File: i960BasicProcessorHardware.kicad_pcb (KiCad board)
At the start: 4 copper layers, 169.9 x 169.8 mm, 72 parts, among them J1 Conn_01x08, J10 Conn_01x03, J11 Conn_01x03, J12 Conn_01x06, J13 Conn_01x11, J14 Conn_02x39_Odd_Even, J4 Conn_02x05_Odd_Even, J5 Conn_02x05_Odd_Even, J6 Conn_02x05_Odd_Even, J9 Conn_02x16_Odd_Even, U1 74HC245, U10 Adafruit_FeatherWing (PSRAM F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, U11 Adafruit_FeatherWing (PSRAM F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, U12 74LS125, U13 74LS04, U14 74LS08, U15 74LS174, U16 SN74LVC245AN, U17 74LS174, U18 ATtiny861-20PU, U19 ATtiny861-20PU, U2 80960Sx, U3 MCP23S17_SP, U4 MCP23S17_SP, U5 74HC245, U6 74HC573, U7 74HC573, U8 MCP23S17_SP, U9 MCP23S17_SP

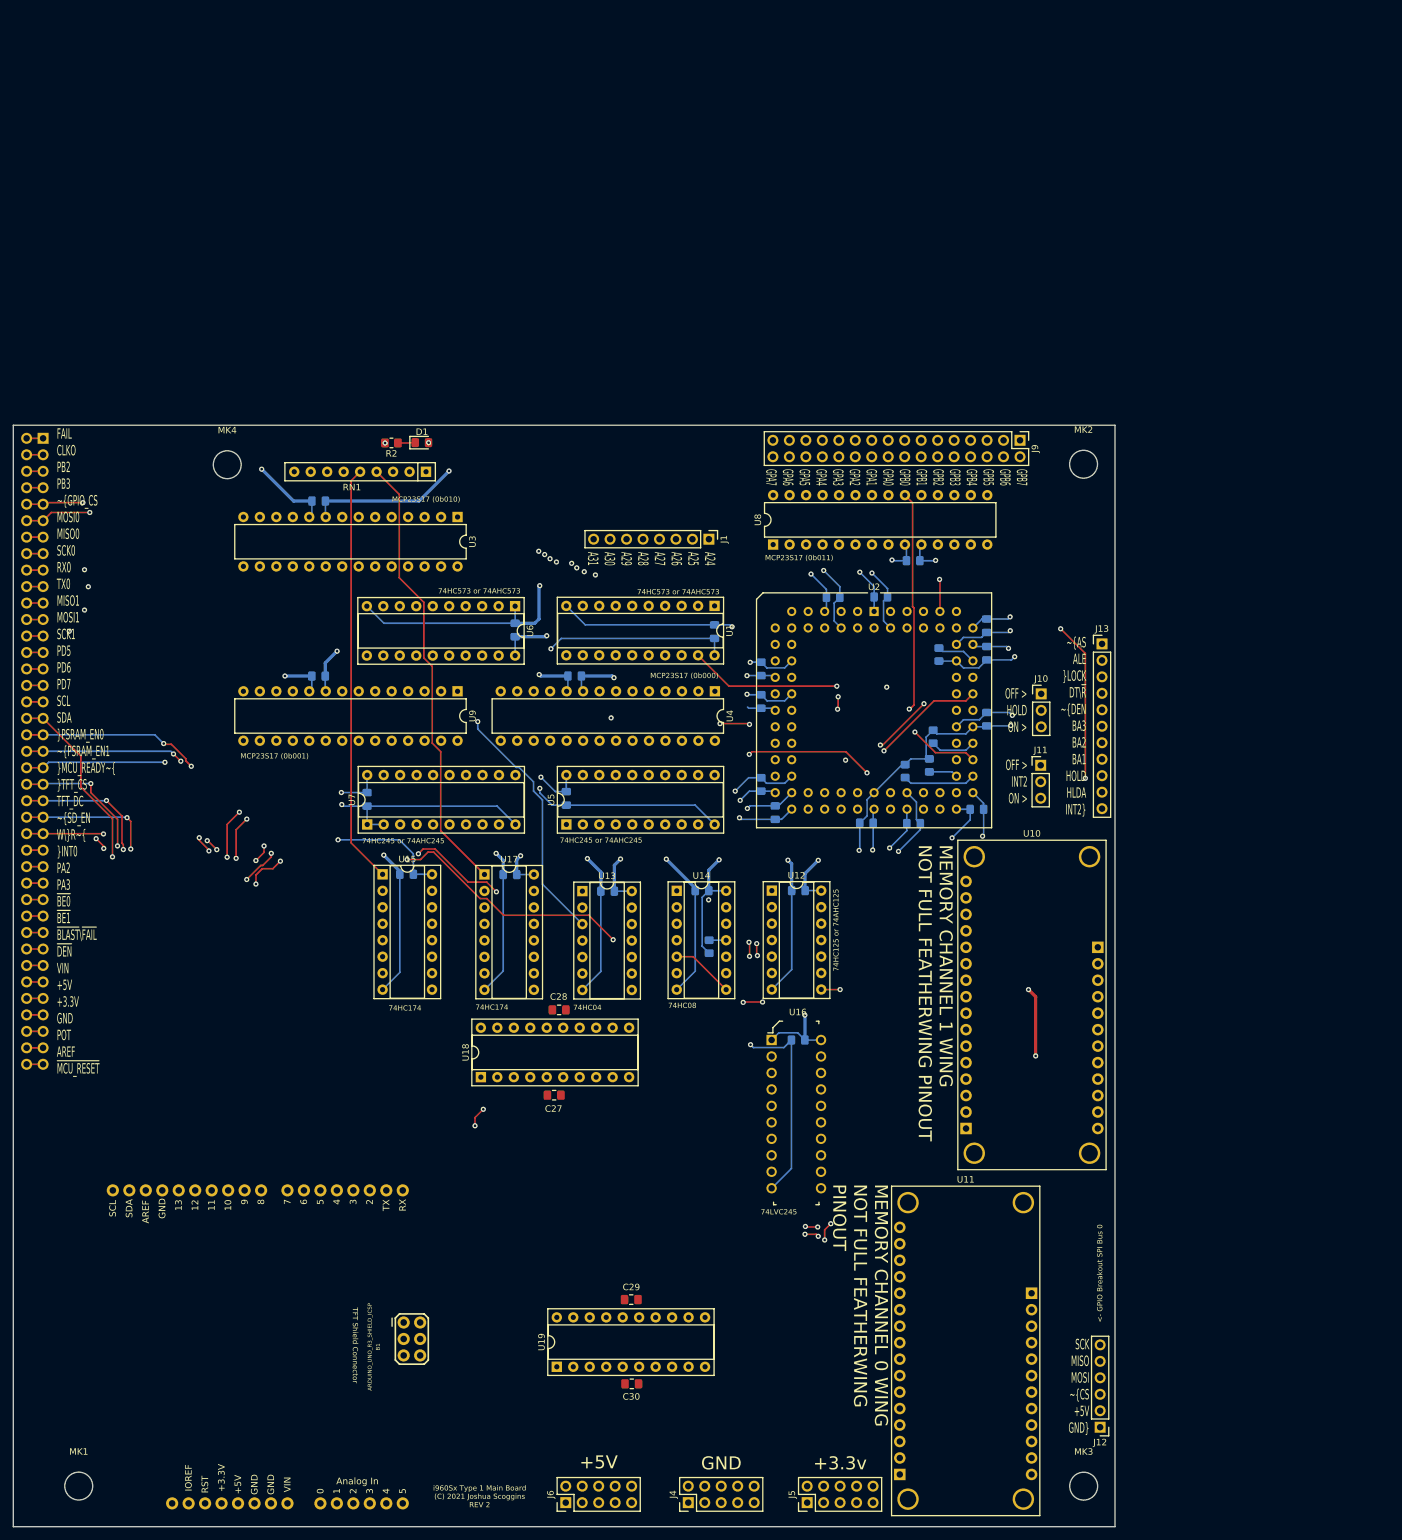
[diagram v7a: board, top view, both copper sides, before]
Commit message: start moving the 74lvc245 to free up some space
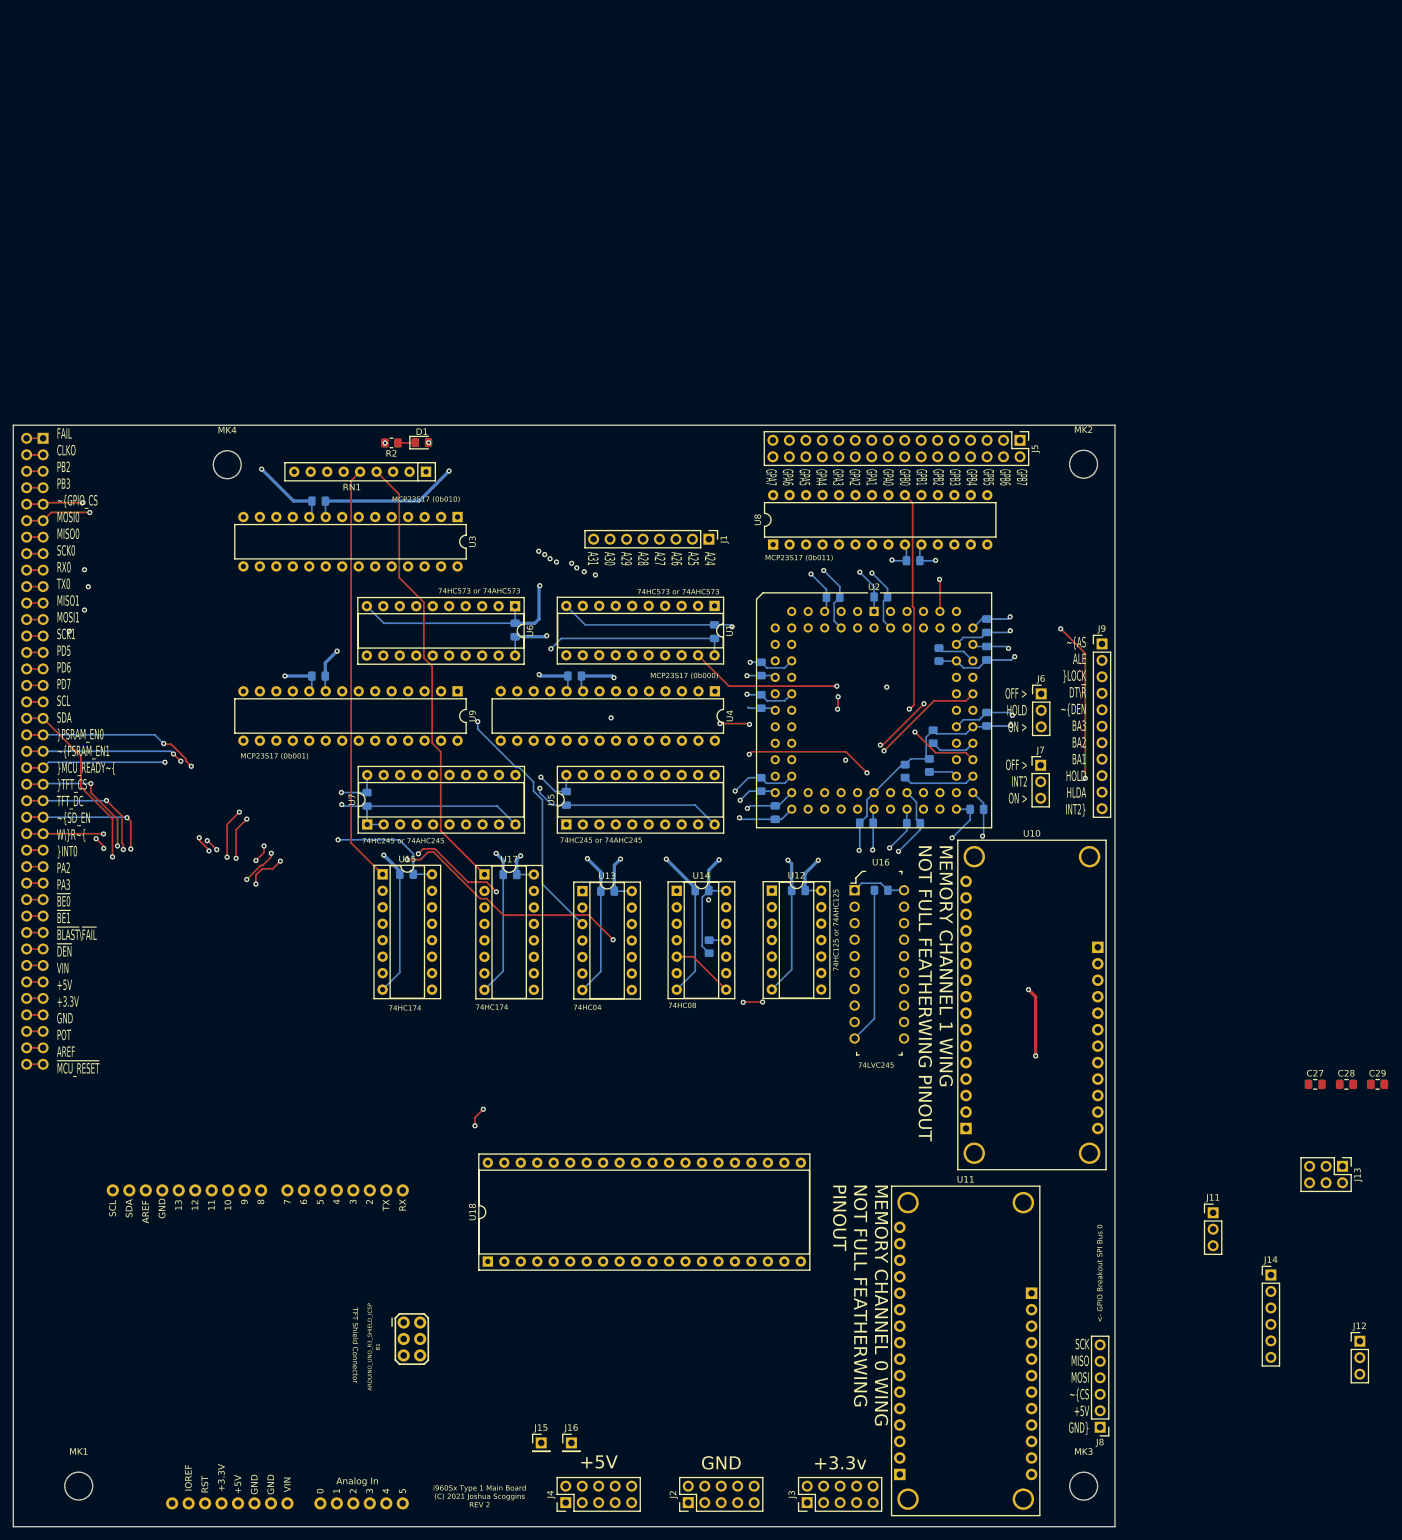
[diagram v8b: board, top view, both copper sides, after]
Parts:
- removed C30: 0.1uF, Capacitor_SMD:C_0805_2012Metric_Pad1.18x1.45mm_HandSolder
- removed U19: ATtiny861-20PU, Package_DIP:DIP-20_W7.62mm_Socket
- added J11: Conn_01x03, Connector_PinHeader_2.54mm:PinHeader_1x03_P2.54mm_Vertical, F.Cu at (202.0, 151.4)
- added J12: Conn_01x03, Connector_PinHeader_2.54mm:PinHeader_1x03_P2.54mm_Vertical, F.Cu at (224.6, 171.2)
- added J13: AVR-ISP-6, Connector_PinHeader_2.54mm:PinHeader_2x03_P2.54mm_Vertical, F.Cu at (221.9, 144.3)
- added J14: Conn_01x06 (Serial Connector), Connector_PinHeader_2.54mm:PinHeader_1x06_P2.54mm_Vertical, F.Cu at (210.9, 161.0)
- added J15: Conn_01x01, Connector_PinHeader_2.54mm:PinHeader_1x01_P2.54mm_Vertical, F.Cu at (98.4, 186.9)
- added J16: Conn_01x01, Connector_PinHeader_2.54mm:PinHeader_1x01_P2.54mm_Vertical, F.Cu at (103.0, 186.9)
- U18: value ATtiny861-20PU -> ATmega1284P-PU; footprint Package_DIP:DIP-20_W7.62mm_Socket -> Package_DIP:DIP-40_W15.24mm_Socket
- moved C28 121.9 mm to (222.5, 131.6), turned to 0 degrees
- moved C29 119.8 mm to (227.3, 131.6), turned to 0 degrees
- moved C27 117.4 mm to (217.7, 131.6)
- moved U18 28.4 mm to (90.1, 158.9)
- moved C22 26.4 mm to (150.8, 101.7)
- moved U16 26.4 mm to (146.7, 101.7)
- renumbered J14 to J10, J4 to J2, J5 to J3, J6 to J4, J9 to J5, J10 to J6, J11 to J7, J12 to J8, J13 to J9
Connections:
- net /Coprocessor0/PA0 renamed /Sheet7D8CCC79/PD6
- net /Coprocessor0/PA1 renamed /Sheet7D8CCC79/PD5
- net /Coprocessor0/PA2 renamed /Sheet7D8CCC79/PD4
- net /Coprocessor0/PA3 renamed /Sheet7D8CCC79/PD3
- net /Coprocessor0/PB0 renamed /Sheet7D8CCC79/PB0
- net /Coprocessor0/PB1 renamed /Sheet7D8CCC79/PB1
- net /Coprocessor0/PB2 renamed /Sheet7D8CCC79/PB2
- net /Coprocessor0/PB3 renamed /Sheet7D8CCC79/PB3
- C27 pad 1: +5V -> Net-(C27-Pad1)
- C29 pad 1: +5V -> Net-(C29-Pad1)
- C29 pad 2: GND -> /Sheet7D8CCC79/~PRG_RESET
- U18 pad 10: /~MCU_RESET -> +5V
- U18 pad 11: /Coprocessor0/PA7 -> GND
- U18 pad 12: /Coprocessor0/PA6 -> GND
- U18 pad 13: /Coprocessor0/PA5 -> /Sheet7D8CCC79/EXTCLK
- U18 pad 14: /Coprocessor0/PA4 -> /Sheet7D8CCC79/PD0
- U18 pad 15: +5V -> /Sheet7D8CCC79/PD1
- U18 pad 16: GND -> /Sheet7D8CCC79/PD2
- U18 pad 5: +5V -> /Sheet7D8CCC79/PB4
- U18 pad 6: GND -> /Sheet7D8CCC79/PB5
- U18 pad 7: /CLKO -> /Sheet7D8CCC79/PB6
- U18 pad 8: GND -> /Sheet7D8CCC79/PB7
- U18 pad 9: /Coprocessor0/PB6 -> /Sheet7D8CCC79/~RESET
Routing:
- net /SCK0: track 460.7 -> 309.3 mm, vias 6 -> 4
- net /MOSI0: track 459.8 -> 310.3 mm, vias 5 -> 3
- net /MISO0: track 442.0 -> 349.2 mm, vias 7 -> 4
- net /3V_MISO0: track 75.8 -> 0.00 mm
- net /~3V_PSRAM_EN2: track 107.3 -> 59.8 mm
- net /~3V_PSRAM_EN1: track 107.9 -> 60.4 mm
- net /SCK1: track 154.6 -> 107.7 mm
- net /MOSI1: track 155.7 -> 110.7 mm
- net /3V_MOSI0: track 44.1 -> 0.00 mm
- net /3V_SCK0: track 44.1 -> 0.00 mm
- net /3V_MISO1: track 33.2 -> 0.00 mm
- net /~PSRAM_EN1: track 151.2 -> 124.4 mm, vias 6 -> 4
- net /3V_MOSI1: track 26.2 -> 0.00 mm
- net /3V_SCK1: track 26.2 -> 0.00 mm
- net /~PSRAM_EN2: track 144.3 -> 118.4 mm, vias 6 -> 4
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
